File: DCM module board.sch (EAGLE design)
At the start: 11 parts, among them X1 5566-10

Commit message: Add files via upload
Version 1.0
- FT, TR circuits added
To complete: PCB layout
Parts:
- added R10, R5, R6, R7, R8, R9: (no value), rcl:R-EU_R0805
- added R3, R4: SLR-56VR3F, SLR-56VR3F:SLR-56VR3F
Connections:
- new net FT1: R6.1, U$1.FAULT
- new net FT2: R7.1, U$2.FAULT
- new net N$6: R3.2, R5.1, R6.2
- new net N$9: R4.2, R7.2, R8.1
- new net TR1: R9.1, U$1.TRIM
- new net TR2: R10.1, U$2.TRIM
- net GND: now also R10.2, R3.1, R4.1, R5.2, R8.2, R9.2
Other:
- moved on the sheet: C1, L1, L2, R1, R2

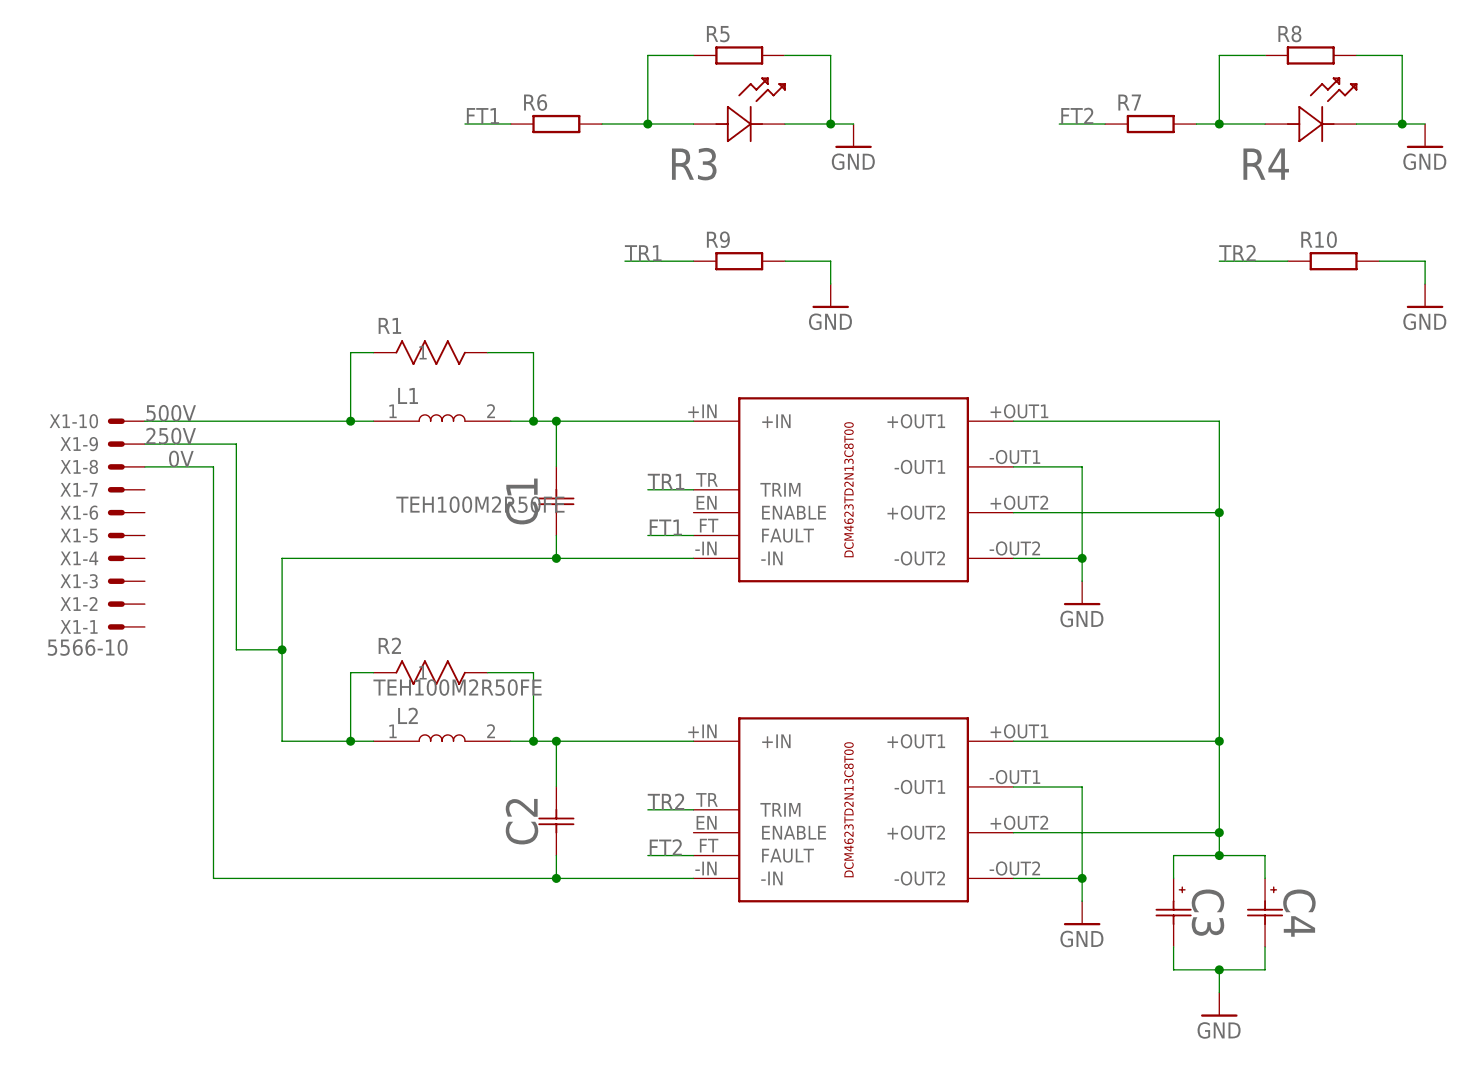
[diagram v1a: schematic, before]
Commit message: Add files via upload
Version 1.1
Changes - changed grounds of FT, TR pin circuits to IN-
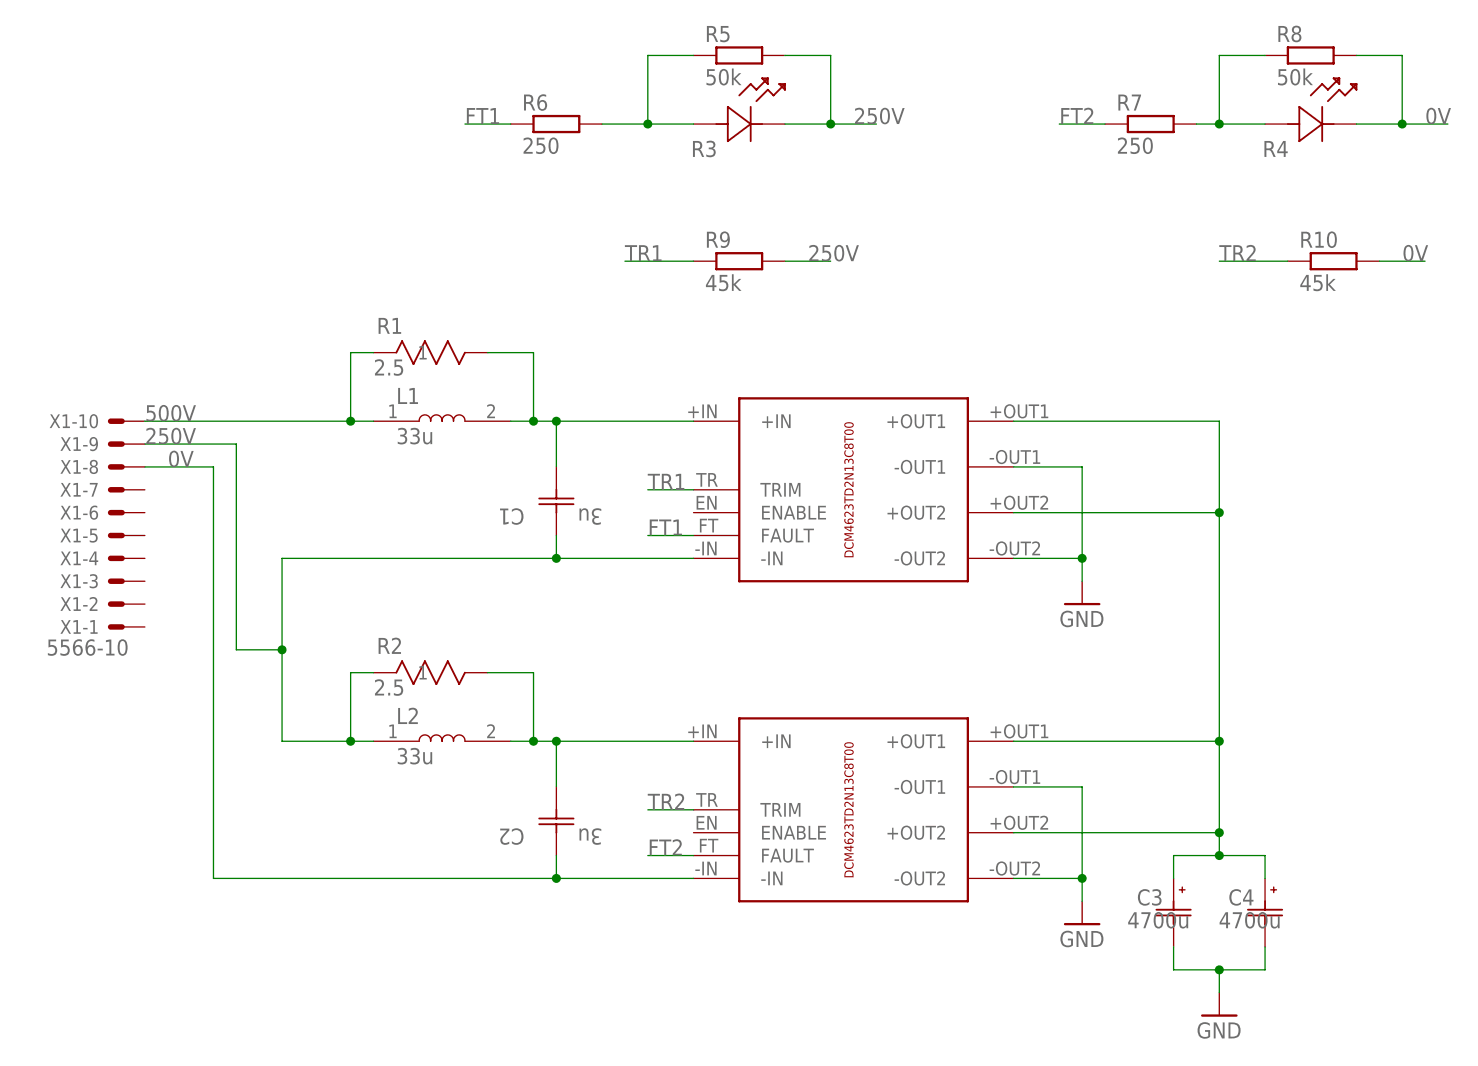
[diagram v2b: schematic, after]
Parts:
- C1, C2: value (none) -> 3u
- C3, C4: value UBY1E472MHL1TN -> 4700u
- L1, L2: value SRP1265A-330M -> 33u
- R1, R2: value TEH100M2R50FE -> 2.5
- R10, R9: value (none) -> 45k
- R5, R8: value (none) -> 50k
- R6, R7: value (none) -> 250
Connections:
- net 0V: now also R10.2, R4.1, R8.2
- net 250V: now also R3.1, R5.2, R9.2
- net GND: no longer R10.2, R3.1, R4.1, R5.2, R8.2, R9.2
